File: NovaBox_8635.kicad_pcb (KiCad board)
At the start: 2 copper layers, 82 x 30 mm, 87 parts, among them P1 MH, P2 MH, P3 MH, P4 MH, P5 USB, Q1 MMBT3904, Q2 IRLML6344, Q3 IRLML6401, Q4 MMBT3904, Q5 MMBT3904, SW1 PIO18, SW2 PIO21, SW3 PIO8, SW4 PIO0, SW5 PIO1, SW6 ON/OFF, U1 MCP6004, U2 CSR8635_MODULE, U3 CSR_DebugSmall, U4 PAM8304, U5 PAM8304, U6 LT1308

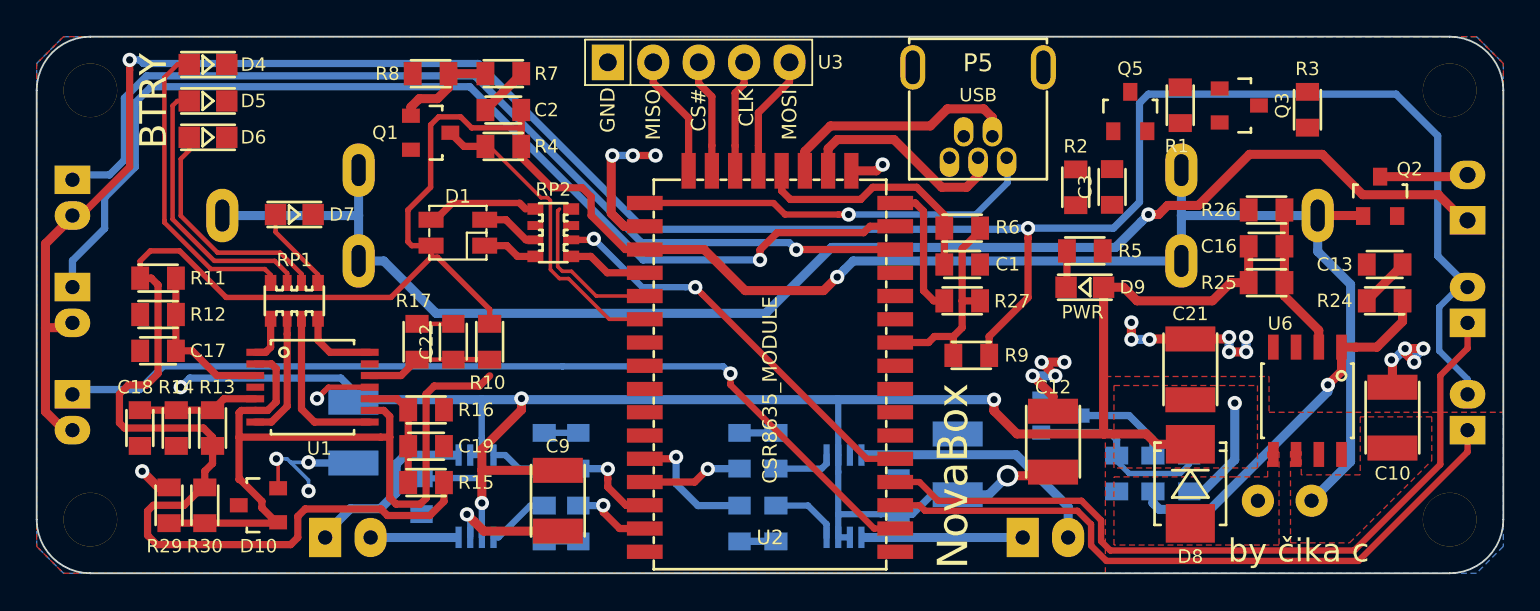
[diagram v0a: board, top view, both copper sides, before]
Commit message: added .gitattribute; small cleanup of PCB; replaced 2mm with 2.5mm pins
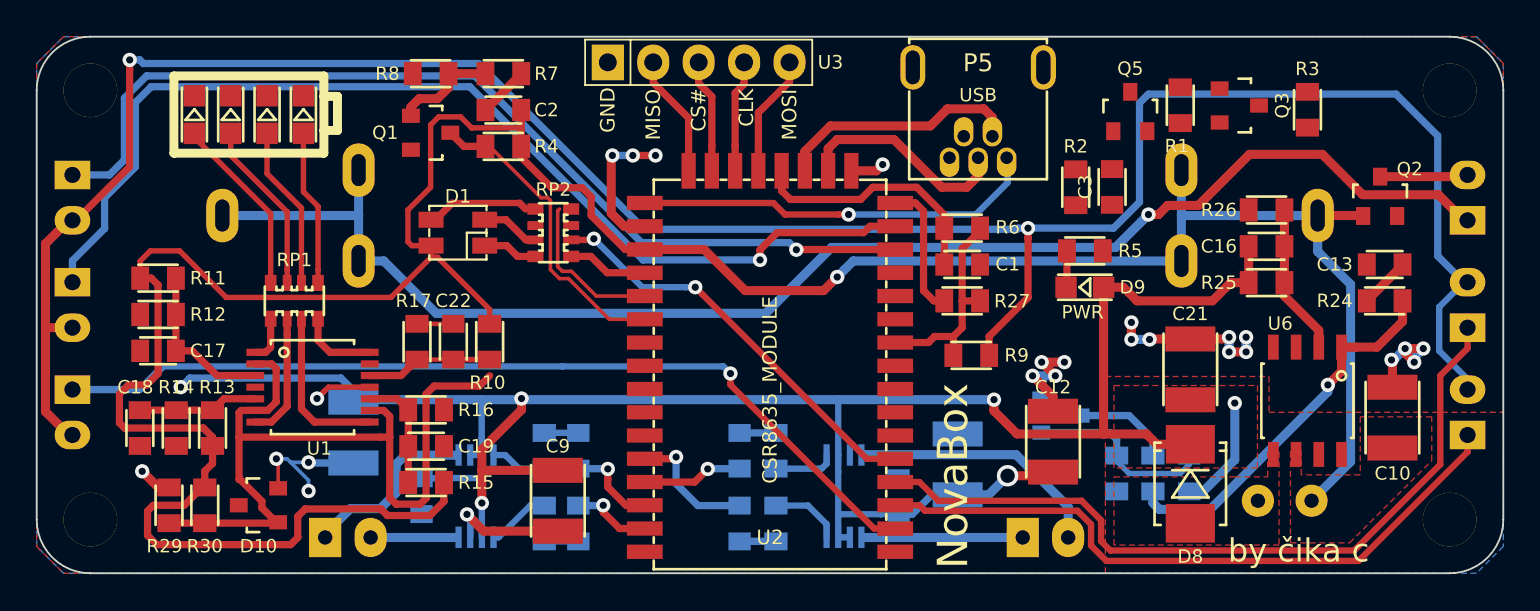
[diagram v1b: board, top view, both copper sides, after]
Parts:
- D7: value TEMP_H -> BATT_E
- R1, R2, R3: value 33K -> 10K
- SW1, SW2, SW3, SW4, SW5: footprint NovaBox:Switch_2mm -> NovaBox:Switch_2.5mm
- moved D7 5.61 mm to (73.9, 54.4), turned to 270 degrees
- moved D6 3.54 mm to (71.9, 54.4), turned to 270 degrees
- moved D4 2.90 mm to (67.8, 54.4), turned to 270 degrees
- moved D5 1.48 mm to (69.8, 54.4), turned to 270 degrees
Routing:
- net Net-(D4-Pad2): track 17.4 -> 10.1 mm
- net Net-(D5-Pad2): track 15.6 -> 9.67 mm
- net Net-(D6-Pad2): track 13.2 -> 9.16 mm
- net Net-(D7-Pad2): track 4.81 -> 8.70 mm
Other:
- board text removed: "BTRY"

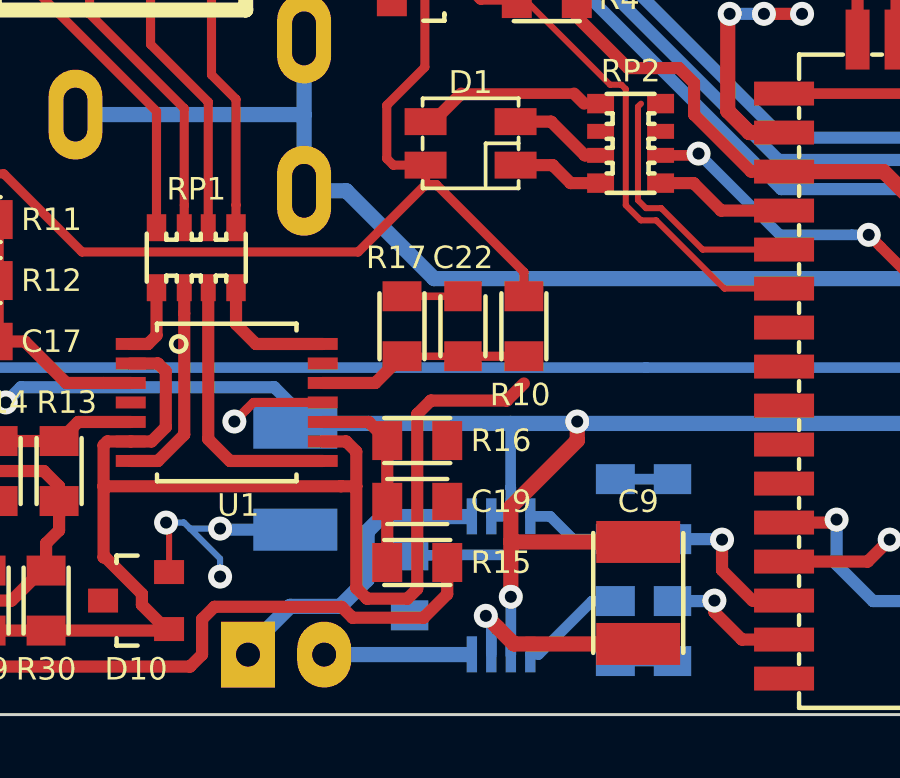
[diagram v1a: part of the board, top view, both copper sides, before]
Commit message: battery LEDs
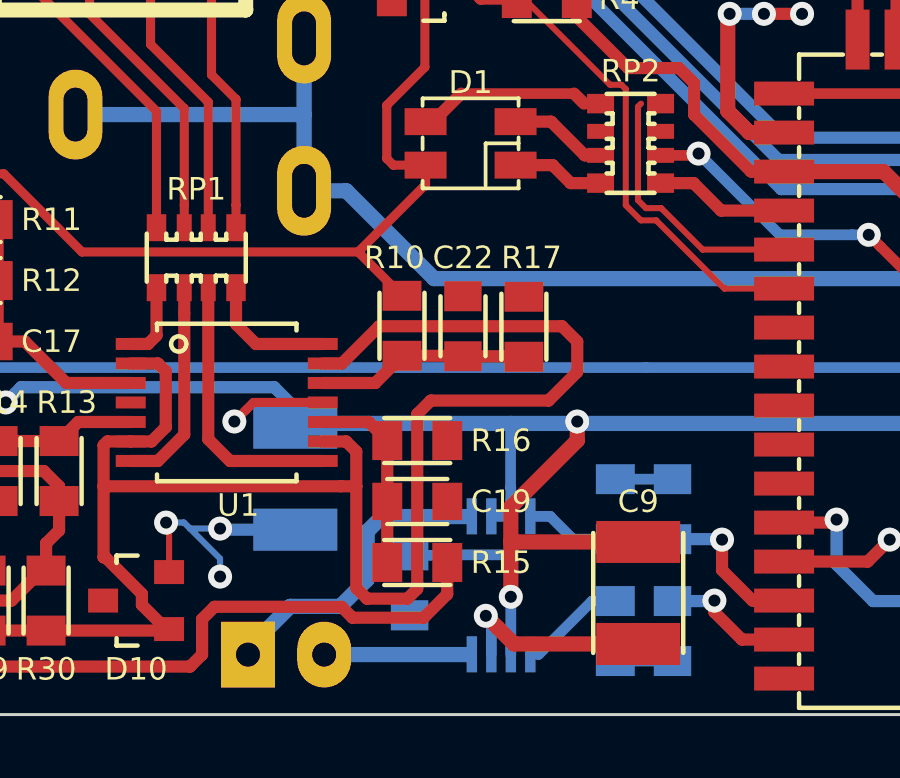
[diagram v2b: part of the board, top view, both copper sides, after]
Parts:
- moved R10 4.06 mm to (80.3, 67.0)
- moved R17 4.06 mm to (84.3, 67.1)
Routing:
- net 2V5: track 45.1 -> 57.2 mm
- net +BATT: track 161.0 -> 157.2 mm
- net GND: track 52.9 -> 50.9 mm
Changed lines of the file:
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@@
     (thickness 1.6)
     (drawings 21)
-    (tracks 646)
+    (tracks 648)
     (zones 0)
     (modules 87)
@@
   )
   (module NovaBox:R_0805 (layer F.Cu)
-    (at 84.328 67.056 90)
+    (at 80.264 67.04 90)
     (descr "Resistor SMD 0805, reflow soldering, Vishay (see dcrcw.pdf)")
     (tags "resistor 0805")
     (attr smd)
-    (fp_text reference R10 (at -2.286 -0.127 -180) (layer F.SilkS)
+    (fp_text reference R10 (at 2.27 -0.254 -180) (layer F.SilkS)
       (effects (font (size 0.75 0.75) (thickness 0.15)))
     )
@@
   )
   (module NovaBox:R_0805 (layer F.Cu)
-    (at 80.264 67.056 90)
+    (at 84.328 67.072 90)
     (descr "Resistor SMD 0805, reflow soldering, Vishay (see dcrcw.pdf)")
     (tags "resistor 0805")
     (attr smd)
-    (fp_text reference R17 (at 2.286 -0.1905 180) (layer F.SilkS)
+    (fp_text reference R17 (at 2.302 0.254 180) (layer F.SilkS)
       (effects (font (size 0.75 0.75) (thickness 0.15)))
     )
@@
   (segment (start 132.461 73.763) (end 130.278 75.946) (width 0.508) (layer B.Cu) (net 1) (status 20))
   (segment (start 132.461 63.849) (end 132.461 73.763) (width 0.508) (layer B.Cu) (net 1))
-  (segment (start 84.178 66.056) (end 84.328 66.056) (width 0.2032) (layer F.Cu) (net 1) (status 30))
-  (segment (start 84.328 66.056) (end 83.931 66.056) (width 0.254) (layer F.Cu) (net 1) (status 30))
   (segment (start 79.973 61.685) (end 81.05 61.685) (width 0.3048) (layer F.Cu) (net 1) (status 20))
   (segment (start 79.756 61.468) (end 79.973 61.685) (width 0.3048) (layer F.Cu) (net 1))
@@
   (segment (start 81.026 54.931918) (end 81.026 58.42) (width 0.3048) (layer F.Cu) (net 1))
   (segment (start 81.026 58.42) (end 79.756 59.69) (width 0.3048) (layer F.Cu) (net 1))
-  (segment (start 81.4098 62.333) (end 81.05 62.333) (width 0.3048) (layer F.Cu) (net 1))
-  (segment (start 84.328 65.2512) (end 81.4098 62.333) (width 0.3048) (layer F.Cu) (net 1))
-  (segment (start 84.328 66.056) (end 84.328 65.2512) (width 0.3048) (layer F.Cu) (net 1) (status 10))
+  (segment (start 78.8035 64.5795) (end 80.264 66.04) (width 0.3048) (layer F.Cu) (net 1))
   (segment (start 139 60.27) (end 138.8 60.27) (width 0.508) (layer F.Cu) (net 2) (status 30))
   (segment (start 130.8735 56.5785) (end 126.8095 56.5785) (width 0.508) (layer F.Cu) (net 2))
@@
   (segment (start 91.842 60.6) (end 91.1225 59.8805) (width 0.508) (layer F.Cu) (net 4))
   (segment (start 93 60.6) (end 91.842 60.6) (width 0.508) (layer F.Cu) (net 4) (status 10))
-  (segment (start 82.296 66.056) (end 80.264 66.056) (width 0.254) (layer F.Cu) (net 4) (status 30))
   (segment (start 86.09 52.07) (end 86.09 52.102) (width 0.508) (layer F.Cu) (net 5) (status 30))
   (segment (start 86.09 52.102) (end 84.09 54.102) (width 0.508) (layer F.Cu) (net 5) (status 30))
@@
   (segment (start 71.5936 75.975122) (end 71.5936 76.3436) (width 0.4064) (layer F.Cu) (net 49))
   (segment (start 71.5936 76.3436) (end 72.4 77.15) (width 0.4064) (layer F.Cu) (net 49) (status 20))
-  (segment (start 78.74 75.779522) (end 78.74 72.39) (width 0.4064) (layer F.Cu) (net 49))
   (segment (start 77.622 70.896) (end 78.403522 70.896) (width 0.4064) (layer F.Cu) (net 49) (status 10))
   (segment (start 78.403522 70.896) (end 78.74 71.232478) (width 0.4064) (layer F.Cu) (net 49))
@@
   (segment (start 72.39 70.422282) (end 71.916282 70.896) (width 0.4064) (layer F.Cu) (net 49))
   (segment (start 71.916282 70.896) (end 71.222 70.896) (width 0.4064) (layer F.Cu) (net 49) (status 20))
-  (segment (start 80.447022 76.1365) (end 79.096978 76.1365) (width 0.4064) (layer F.Cu) (net 49))
-  (segment (start 79.096978 76.1365) (end 78.74 75.779522) (width 0.4064) (layer F.Cu) (net 49))
-  (segment (start 80.772 69.984478) (end 80.772 75.811522) (width 0.4064) (layer F.Cu) (net 49))
-  (segment (start 84.328 68.9624) (end 83.7579 69.5325) (width 0.4064) (layer F.Cu) (net 49))
-  (segment (start 83.7579 69.5325) (end 81.223978 69.5325) (width 0.4064) (layer F.Cu) (net 49))
-  (segment (start 81.223978 69.5325) (end 80.772 69.984478) (width 0.4064) (layer F.Cu) (net 49))
-  (segment (start 80.772 75.811522) (end 80.447022 76.1365) (width 0.4064) (layer F.Cu) (net 49))
+  (segment (start 78.262 68.296) (end 77.622 68.296) (width 0.4064) (layer F.Cu) (net 49))
+  (segment (start 79.502 67.056) (end 78.262 68.296) (width 0.4064) (layer F.Cu) (net 49))
+  (segment (start 86.106 68.58) (end 86.106 67.564) (width 0.4064) (layer F.Cu) (net 49))
+  (segment (start 85.1535 69.5325) (end 86.106 68.58) (width 0.4064) (layer F.Cu) (net 49))
+  (segment (start 81.223978 69.5325) (end 85.1535 69.5325) (width 0.4064) (layer F.Cu) (net 49))
+  (segment (start 78.74 75.779522) (end 79.096978 76.1365) (width 0.4064) (layer F.Cu) (net 49))
+  (segment (start 86.106 67.564) (end 85.598 67.056) (width 0.4064) (layer F.Cu) (net 49))
+  (segment (start 78.74 72.39) (end 78.74 75.779522) (width 0.4064) (layer F.Cu) (net 49))
+  (segment (start 79.096978 76.1365) (end 80.447022 76.1365) (width 0.4064) (layer F.Cu) (net 49))
+  (segment (start 80.447022 76.1365) (end 80.772 75.811522) (width 0.4064) (layer F.Cu) (net 49))
+  (segment (start 80.772 75.811522) (end 80.772 69.984478) (width 0.4064) (layer F.Cu) (net 49))
+  (segment (start 85.598 67.056) (end 79.502 67.056) (width 0.4064) (layer F.Cu) (net 49))
+  (segment (start 80.772 69.984478) (end 81.223978 69.5325) (width 0.4064) (layer F.Cu) (net 49))
   (segment (start 104.394 59.944) (end 111.506 59.944) (width 0.3556) (layer B.Cu) (net 50))
   (segment (start 111.506 59.944) (end 113.284 58.166) (width 0.3556) (layer B.Cu) (net 50))
@@
   (segment (start 80.264 68.056) (end 79.374 68.946) (width 0.4064) (layer F.Cu) (net 68) (status 10))
   (segment (start 79.374 68.946) (end 77.622 68.946) (width 0.4064) (layer F.Cu) (net 68) (status 20))
-  (segment (start 80.264 68.056) (end 82.296 68.056) (width 0.254) (layer F.Cu) (net 68) (status 30))
-  (segment (start 82.296 68.056) (end 84.328 68.056) (width 0.3048) (layer F.Cu) (net 68) (status 30))
+  (segment (start 82.28 68.04) (end 82.296 68.056) (width 0.4064) (layer F.Cu) (net 68))
+  (segment (start 80.264 68.04) (end 82.28 68.04) (width 0.4064) (layer F.Cu) (net 68))
+  (segment (start 84.312 68.056) (end 84.328 68.072) (width 0.4064) (layer F.Cu) (net 68))
+  (segment (start 82.296 68.056) (end 84.312 68.056) (width 0.4064) (layer F.Cu) (net 68))
   (zone (net 0) (net_name "") (layer B.Cu) (hatch edge 0.508)
     (connect_pads (clearance 0.254))

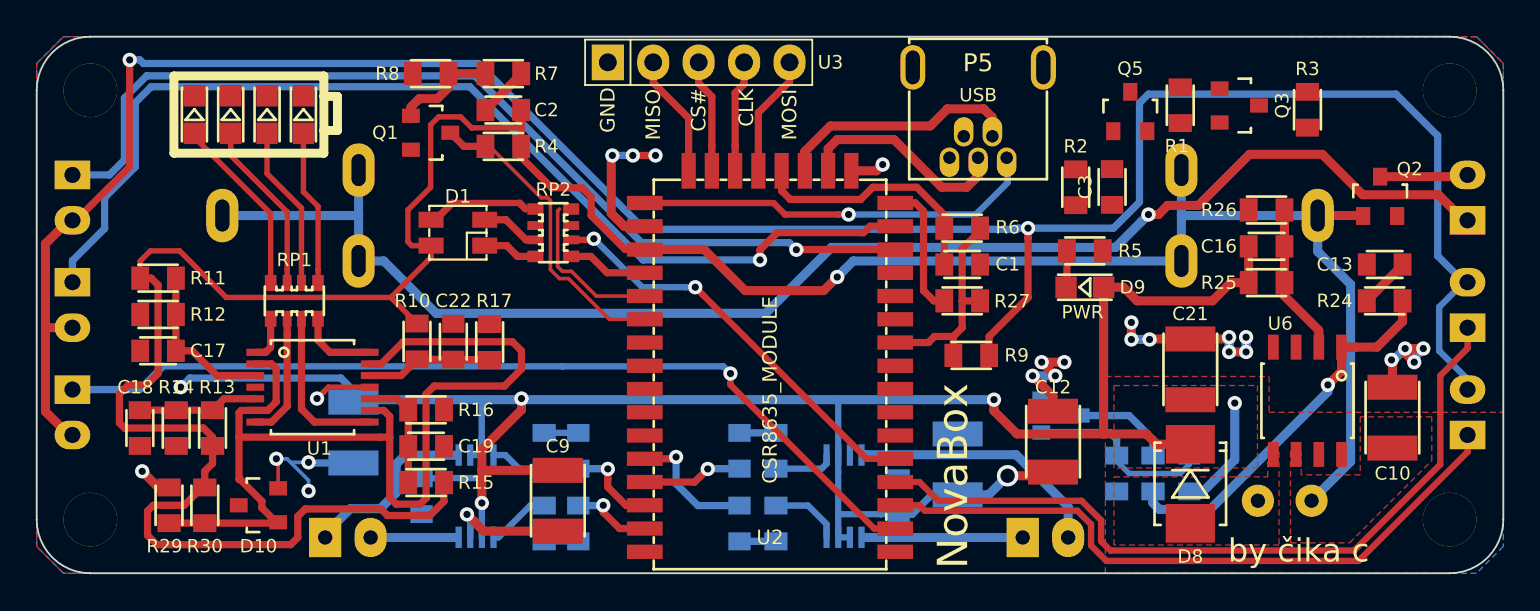
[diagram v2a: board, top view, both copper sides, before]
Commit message: renamed .gitattributes; added power LTspice sim
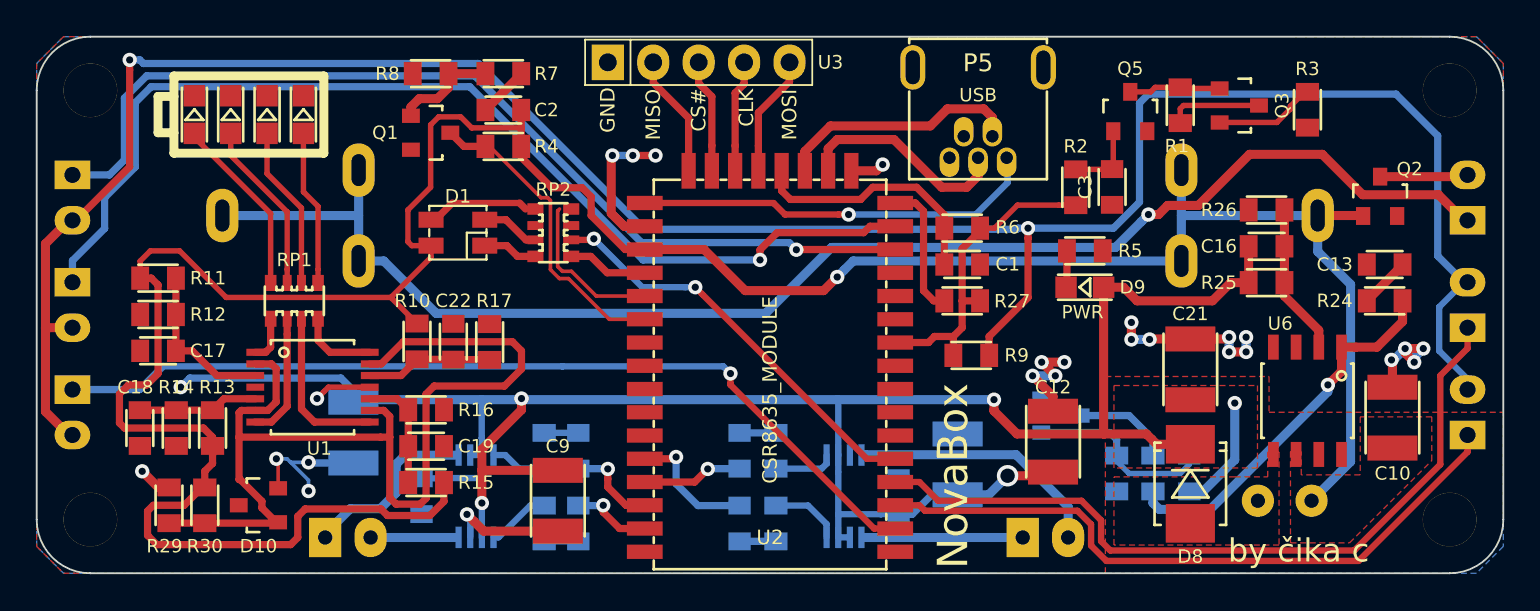
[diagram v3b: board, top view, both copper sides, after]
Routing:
- net 1V8: track 12.3 -> 18.2 mm
- net VR_SHDN: track 0.00 -> 5.71 mm
- net +BATT: track 157.2 -> 162.5 mm
- net Net-(Q3-Pad1): track 0.00 -> 5.13 mm
- net Net-(C3-Pad2): track 0.00 -> 4.18 mm
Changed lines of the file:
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@@
     (thickness 1.6)
     (drawings 21)
-    (tracks 648)
+    (tracks 669)
     (zones 0)
     (modules 87)
@@
     )
   )
-  (gr_line (start 75.819 55.245) (end 75.057 55.245) (angle 90) (layer F.SilkS) (width 0.5))
-  (gr_line (start 75.819 53.34) (end 75.819 55.245) (angle 90) (layer F.SilkS) (width 0.5))
-  (gr_line (start 75.057 53.34) (end 75.819 53.34) (angle 90) (layer F.SilkS) (width 0.5))
+  (gr_line (start 65.786 55.372) (end 66.675 55.372) (layer F.SilkS) (width 0.5))
+  (gr_line (start 66.675 53.34) (end 65.786 53.34) (layer F.SilkS) (width 0.5))
+  (gr_line (start 65.786 53.34) (end 65.786 55.372) (layer F.SilkS) (width 0.5))
   (gr_line (start 75.057 56.515) (end 75.057 52.197) (angle 90) (layer F.SilkS) (width 0.5))
   (gr_line (start 66.675 56.515) (end 75.057 56.515) (angle 90) (layer F.SilkS) (width 0.5))
@@
   (segment (start 81.026 58.42) (end 79.756 59.69) (width 0.3048) (layer F.Cu) (net 1))
   (segment (start 78.8035 64.5795) (end 80.264 66.04) (width 0.3048) (layer F.Cu) (net 1))
+  (segment (start 122.936 54.0272) (end 122.936 54.832) (width 0.3048) (layer F.Cu) (net 1))
+  (segment (start 123.1152 53.848) (end 122.936 54.0272) (width 0.3048) (layer F.Cu) (net 1))
+  (segment (start 127.338 53.848) (end 123.1152 53.848) (width 0.3048) (layer F.Cu) (net 1))
   (segment (start 139 60.27) (end 138.8 60.27) (width 0.508) (layer F.Cu) (net 2) (status 30))
   (segment (start 130.8735 56.5785) (end 126.8095 56.5785) (width 0.508) (layer F.Cu) (net 2))
@@
   (segment (start 111.744 64.77) (end 111.744 64.92) (width 0.4064) (layer F.Cu) (net 6) (status 30))
   (segment (start 110.252 67.818) (end 110.252 67.802) (width 0.254) (layer F.Cu) (net 6) (status 30))
+  (segment (start 116.1392 59.42) (end 117.094 59.42) (width 0.3048) (layer F.Cu) (net 6))
+  (segment (start 113.8348 59.42) (end 116.1392 59.42) (width 0.3048) (layer F.Cu) (net 6))
+  (segment (start 112.5488 60.706) (end 113.8348 59.42) (width 0.3048) (layer F.Cu) (net 6))
+  (segment (start 111.744 60.706) (end 112.5488 60.706) (width 0.3048) (layer F.Cu) (net 6))
   (segment (start 87.376 78.216) (end 89.281 78.216) (width 0.3556) (layer B.Cu) (net 7) (status 30))
   (segment (start 90.678 76.5844) (end 90.678 76.2) (width 0.4064) (layer F.Cu) (net 8))
@@
   (segment (start 116.602 61.976) (end 116.602 63.958) (width 0.4064) (layer F.Cu) (net 65) (status 30))
   (segment (start 116.602 63.958) (end 116.552 64.008) (width 0.4064) (layer F.Cu) (net 65) (status 30))
+  (segment (start 129.898 53.086) (end 130.048 53.086) (width 0.3048) (layer F.Cu) (net 66))
+  (segment (start 129.0932 53.8908) (end 129.898 53.086) (width 0.3048) (layer F.Cu) (net 66))
+  (segment (start 129.0932 54.0408) (end 129.0932 53.8908) (width 0.3048) (layer F.Cu) (net 66))
+  (segment (start 128.336 54.798) (end 129.0932 54.0408) (width 0.3048) (layer F.Cu) (net 66))
+  (segment (start 125.138 54.798) (end 128.336 54.798) (width 0.3048) (layer F.Cu) (net 66))
+  (segment (start 119.192 57.338) (end 119.126 57.404) (width 0.3048) (layer F.Cu) (net 67))
+  (segment (start 119.192 55.286) (end 119.192 57.338) (width 0.3048) (layer F.Cu) (net 67))
+  (segment (start 119.11 57.42) (end 119.126 57.404) (width 0.3048) (layer F.Cu) (net 67))
+  (segment (start 117.094 57.42) (end 119.11 57.42) (width 0.3048) (layer F.Cu) (net 67))
   (segment (start 80.264 68.056) (end 79.374 68.946) (width 0.4064) (layer F.Cu) (net 68) (status 10))
   (segment (start 79.374 68.946) (end 77.622 68.946) (width 0.4064) (layer F.Cu) (net 68) (status 20))
@@
   (segment (start 84.312 68.056) (end 84.328 68.072) (width 0.4064) (layer F.Cu) (net 68))
   (segment (start 82.296 68.056) (end 84.312 68.056) (width 0.4064) (layer F.Cu) (net 68))
+  (segment (start 122.936 52.832) (end 121.539 52.832) (width 0.3048) (layer F.Cu) (net 69))
+  (segment (start 121.285 53.086) (end 120.142 53.086) (width 0.3048) (layer F.Cu) (net 69))
+  (segment (start 121.539 52.832) (end 121.285 53.086) (width 0.3048) (layer F.Cu) (net 69))
+  (segment (start 123.002 52.898) (end 122.936 52.832) (width 0.3048) (layer F.Cu) (net 69))
+  (segment (start 125.138 52.898) (end 123.002 52.898) (width 0.3048) (layer F.Cu) (net 69))
   (zone (net 0) (net_name "") (layer B.Cu) (hatch edge 0.508)
     (connect_pads (clearance 0.254))
